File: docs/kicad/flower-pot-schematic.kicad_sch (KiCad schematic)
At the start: 14 parts, among them J1 Raspberry_Pi_2_3, K1 SRD-05VDC-SL-C, M1 Motor_DC, SW1 SW_Push, U1 MCP3202, U2 DHT11, U3 keyestudio_Ks0049

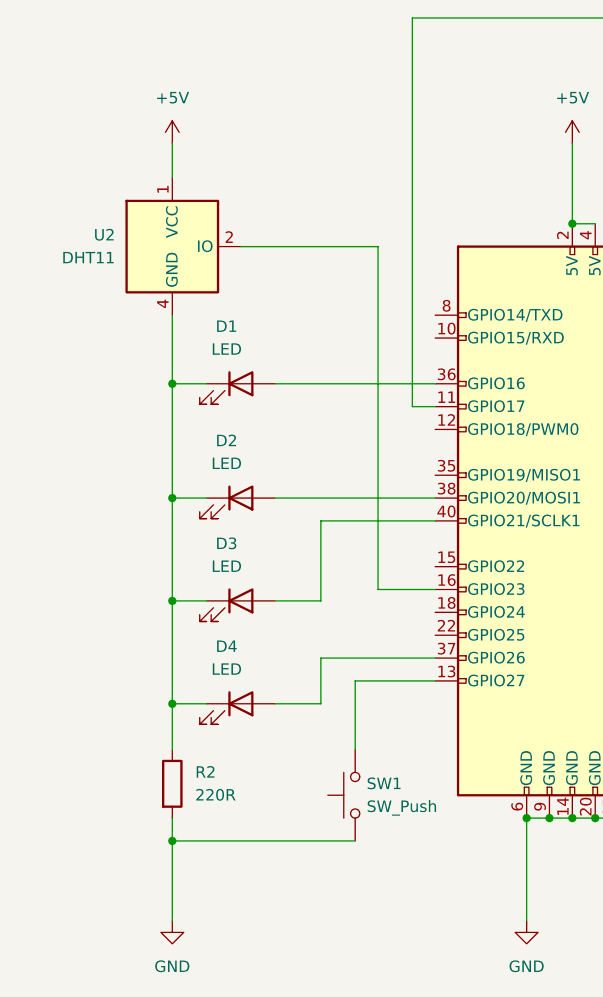
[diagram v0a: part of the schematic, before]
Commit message: fix bad connection on u2
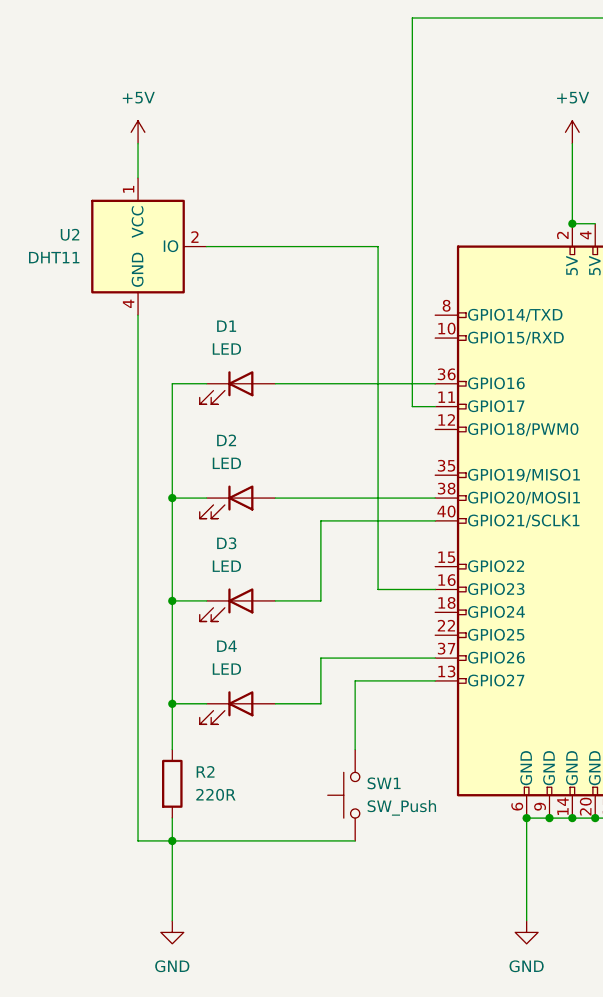
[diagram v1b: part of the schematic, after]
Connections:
- net GND: now also U2.4 (GND)
- net at D1.1 (K), D2.1 (K), D3.1 (K)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: no longer U2.4 (GND)
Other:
- moved on the sheet: U2
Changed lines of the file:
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@@
   (junction (at 81.28 41.91) (diameter 0) (color 0 0 0 0)
   )
-  (junction (at 29.21 59.69) (diameter 0) (color 0 0 0 0)
-  )
   (junction (at 118.11 45.72) (diameter 0) (color 0 0 0 0)
   )
@@
     (stroke (width 0) (type default) (color 0 0 0 0))
   )
-  (wire (pts (xy 29.21 33.02) (xy 29.21 36.83))
+  (wire (pts (xy 25.4 33.02) (xy 25.4 36.83))
     (stroke (width 0) (type default) (color 0 0 0 0))
   )
@@
     (stroke (width 0) (type default) (color 0 0 0 0))
   )
+  (wire (pts (xy 25.4 110.49) (xy 29.21 110.49))
+    (stroke (width 0) (type default) (color 0 0 0 0))
+  )
   (wire (pts (xy 137.16 97.79) (xy 137.16 107.95))
     (stroke (width 0) (type default) (color 0 0 0 0))
@@
     (stroke (width 0) (type default) (color 0 0 0 0))
   )
+  (wire (pts (xy 25.4 52.07) (xy 25.4 110.49))
+    (stroke (width 0) (type default) (color 0 0 0 0))
+  )
   (wire (pts (xy 29.21 107.95) (xy 29.21 110.49))
     (stroke (width 0) (type default) (color 0 0 0 0))
   )
-  (wire (pts (xy 36.83 44.45) (xy 52.07 44.45))
+  (wire (pts (xy 33.02 44.45) (xy 52.07 44.45))
     (stroke (width 0) (type default) (color 0 0 0 0))
   )
@@
   )
   (wire (pts (xy 58.42 92.71) (xy 49.53 92.71))
-    (stroke (width 0) (type default) (color 0 0 0 0))
-  )
-  (wire (pts (xy 29.21 52.07) (xy 29.21 59.69))
     (stroke (width 0) (type default) (color 0 0 0 0))
   )
@@
     (pin "2")
   )
-  (symbol (lib_id "power:+5V") (at 29.21 33.02 0) (unit 1)
-    (in_bom yes) (on_board yes) (fields_autoplaced)
-    (property "Reference" "#PWR?" (id 0) (at 29.21 36.83 0)
-      (effects (font (size 1.27 1.27)) hide)
-    )
-    (property "Value" "+5V" (id 1) (at 29.21 27.94 0))
-    (property "Footprint" "" (id 2) (at 29.21 33.02 0)
-      (effects (font (size 1.27 1.27)) hide)
-    )
-    (property "Datasheet" "" (id 3) (at 29.21 33.02 0)
-      (effects (font (size 1.27 1.27)) hide)
-    )
-    (pin "1")
-  )
-  (symbol (lib_id "Sensor:DHT11") (at 29.21 44.45 0) (unit 1)
-    (in_bom yes) (on_board yes) (fields_autoplaced)
-    (property "Reference" "U2" (id 0) (at 22.86 43.1799 0)
-      (effects (font (size 1.27 1.27)) (justify right))
-    )
-    (property "Value" "DHT11" (id 1) (at 22.86 45.7199 0)
-      (effects (font (size 1.27 1.27)) (justify right))
-    )
-    (property "Footprint" "Sensor:Aosong_DHT11_5.5x12.0_P2.54mm" (id 2) (at 29.21 54.61 0)
-      (effects (font (size 1.27 1.27)) hide)
-    )
-    (property "Datasheet" "http://akizukidenshi.com/download/ds/aosong/DHT11.pdf" (id 3) (at 33.02 38.1 0)
-      (effects (font (size 1.27 1.27)) hide)
-    )
+  (symbol (lib_id "power:+5V") (at 25.4 33.02 0) (unit 1)
+    (in_bom yes) (on_board yes) (fields_autoplaced)
+    (property "Reference" "#PWR?" (id 0) (at 25.4 36.83 0)
+      (effects (font (size 1.27 1.27)) hide)
+    )
+    (property "Value" "+5V" (id 1) (at 25.4 27.94 0))
+    (property "Footprint" "" (id 2) (at 25.4 33.02 0)
+      (effects (font (size 1.27 1.27)) hide)
+    )
+    (property "Datasheet" "" (id 3) (at 25.4 33.02 0)
+      (effects (font (size 1.27 1.27)) hide)
+    )
+    (pin "1")
+  )
+  (symbol (lib_id "Sensor:DHT11") (at 25.4 44.45 0) (unit 1)
+    (in_bom yes) (on_board yes) (fields_autoplaced)
+    (property "Reference" "U2" (id 0) (at 19.05 43.1799 0)
+      (effects (font (size 1.27 1.27)) (justify right))
+    )
+    (property "Value" "DHT11" (id 1) (at 19.05 45.7199 0)
+      (effects (font (size 1.27 1.27)) (justify right))
+    )
+    (property "Footprint" "Sensor:Aosong_DHT11_5.5x12.0_P2.54mm" (id 2) (at 25.4 54.61 0)
+      (effects (font (size 1.27 1.27)) hide)
+    )
+    (property "Datasheet" "http://akizukidenshi.com/download/ds/aosong/DHT11.pdf" (id 3) (at 29.21 38.1 0)
+      (effects (font (size 1.27 1.27)) hide)
+    )

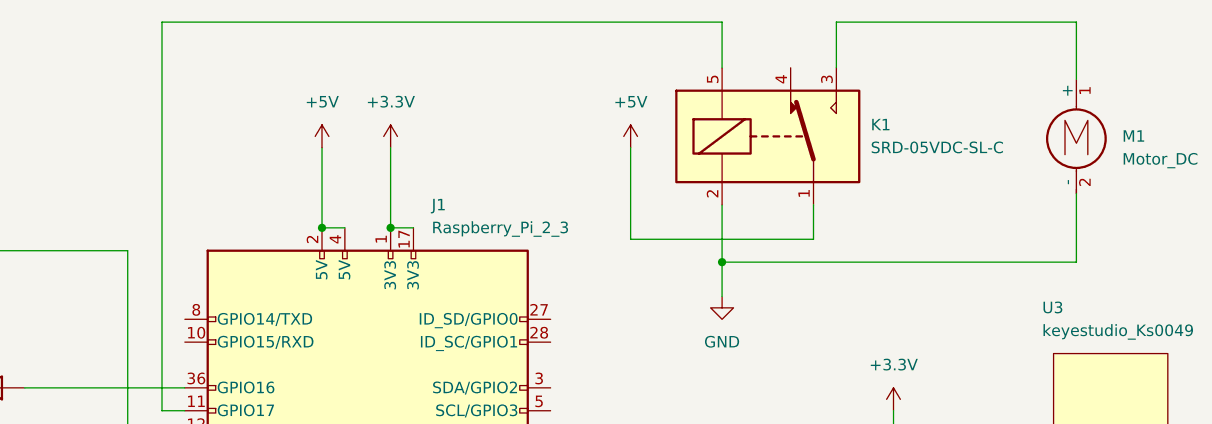
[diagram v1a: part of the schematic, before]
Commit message: add diode to relay, add database, fix element missing error
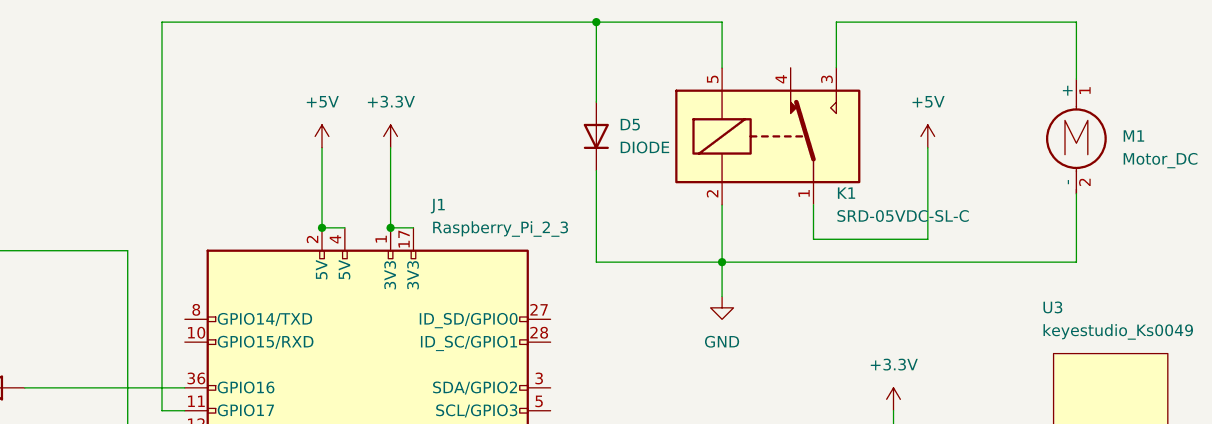
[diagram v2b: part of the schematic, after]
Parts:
- added D5: DIODE, symbol Simulation_SPICE:DIODE
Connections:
- net GND: now also D5.2 (K)
- net at J1.11 (GPIO17), K1.5: now also D5.1 (A)
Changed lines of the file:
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@@
   (junction (at 71.12 107.95) (diameter 0) (color 0 0 0 0)
   )
+  (junction (at 104.14 19.05) (diameter 0) (color 0 0 0 0)
+  )
   (junction (at 175.26 78.74) (diameter 0) (color 0 0 0 0)
   )
@@
     (stroke (width 0) (type default) (color 0 0 0 0))
   )
-  (wire (pts (xy 55.88 19.05) (xy 118.11 19.05))
+  (wire (pts (xy 55.88 19.05) (xy 104.14 19.05))
     (stroke (width 0) (type default) (color 0 0 0 0))
   )
@@
     (stroke (width 0) (type default) (color 0 0 0 0))
   )
+  (wire (pts (xy 104.14 45.72) (xy 118.11 45.72))
+    (stroke (width 0) (type default) (color 0 0 0 0))
+  )
   (wire (pts (xy 118.11 39.37) (xy 118.11 45.72))
     (stroke (width 0) (type default) (color 0 0 0 0))
@@
     (stroke (width 0) (type default) (color 0 0 0 0))
   )
-  (wire (pts (xy 107.95 43.18) (xy 107.95 33.02))
+  (wire (pts (xy 140.97 43.18) (xy 140.97 33.02))
     (stroke (width 0) (type default) (color 0 0 0 0))
   )
@@
     (stroke (width 0) (type default) (color 0 0 0 0))
   )
+  (wire (pts (xy 104.14 19.05) (xy 104.14 27.94))
+    (stroke (width 0) (type default) (color 0 0 0 0))
+  )
   (wire (pts (xy 106.68 80.01) (xy 106.68 90.17))
     (stroke (width 0) (type default) (color 0 0 0 0))
@@
     (stroke (width 0) (type default) (color 0 0 0 0))
   )
+  (wire (pts (xy 104.14 35.56) (xy 104.14 45.72))
+    (stroke (width 0) (type default) (color 0 0 0 0))
+  )
   (wire (pts (xy 29.21 59.69) (xy 33.02 59.69))
     (stroke (width 0) (type default) (color 0 0 0 0))
   )
+  (wire (pts (xy 104.14 19.05) (xy 118.11 19.05))
+    (stroke (width 0) (type default) (color 0 0 0 0))
+  )
   (wire (pts (xy 149.86 90.17) (xy 156.21 90.17))
     (stroke (width 0) (type default) (color 0 0 0 0))
@@
     (stroke (width 0) (type default) (color 0 0 0 0))
   )
-  (wire (pts (xy 128.27 43.18) (xy 107.95 43.18))
+  (wire (pts (xy 128.27 43.18) (xy 140.97 43.18))
     (stroke (width 0) (type default) (color 0 0 0 0))
   )
@@
   )
   (symbol (lib_id "Relay:SANYOU_SRD_Form_C") (at 123.19 31.75 0) (unit 1)
-    (in_bom yes) (on_board yes) (fields_autoplaced)
-    (property "Reference" "K1" (id 0) (at 134.62 30.4799 0)
-      (effects (font (size 1.27 1.27)) (justify left))
-    )
-    (property "Value" "SRD-05VDC-SL-C" (id 1) (at 134.62 33.0199 0)
+    (in_bom yes) (on_board yes)
+    (property "Reference" "K1" (id 0) (at 130.81 38.1 0)
+      (effects (font (size 1.27 1.27)) (justify left))
+    )
+    (property "Value" "SRD-05VDC-SL-C" (id 1) (at 130.81 40.64 0)
       (effects (font (size 1.27 1.27)) (justify left))
     )
@@
     (pin "2")
   )
-  (symbol (lib_id "power:+5V") (at 107.95 33.02 0) (unit 1)
-    (in_bom yes) (on_board yes) (fields_autoplaced)
-    (property "Reference" "#PWR?" (id 0) (at 107.95 36.83 0)
-      (effects (font (size 1.27 1.27)) hide)
-    )
-    (property "Value" "+5V" (id 1) (at 107.95 27.94 0))
-    (property "Footprint" "" (id 2) (at 107.95 33.02 0)
-      (effects (font (size 1.27 1.27)) hide)
-    )
-    (property "Datasheet" "" (id 3) (at 107.95 33.02 0)
+  (symbol (lib_id "power:+5V") (at 140.97 33.02 0) (unit 1)
+    (in_bom yes) (on_board yes) (fields_autoplaced)
+    (property "Reference" "#PWR?" (id 0) (at 140.97 36.83 0)
+      (effects (font (size 1.27 1.27)) hide)
+    )
+    (property "Value" "+5V" (id 1) (at 140.97 27.94 0))
+    (property "Footprint" "" (id 2) (at 140.97 33.02 0)
+      (effects (font (size 1.27 1.27)) hide)
+    )
+    (property "Datasheet" "" (id 3) (at 140.97 33.02 0)
       (effects (font (size 1.27 1.27)) hide)
     )
@@
     (pin "")
   )
+  (symbol (lib_id "Simulation_SPICE:DIODE") (at 104.14 31.75 270) (unit 1)
+    (in_bom yes) (on_board yes) (fields_autoplaced)
+    (property "Reference" "D5" (id 0) (at 106.68 30.4799 90)
+      (effects (font (size 1.27 1.27)) (justify left))
+    )
+    (property "Value" "DIODE" (id 1) (at 106.68 33.0199 90)
+      (effects (font (size 1.27 1.27)) (justify left))
+    )
+    (property "Footprint" "" (id 2) (at 104.14 31.75 0)
+      (effects (font (size 1.27 1.27)) hide)
+    )
+    (property "Datasheet" "~" (id 3) (at 104.14 31.75 0)
+      (effects (font (size 1.27 1.27)) hide)
+    )
+    (property "Spice_Netlist_Enabled" "Y" (id 4) (at 104.14 31.75 0)
+      (effects (font (size 1.27 1.27)) (justify left) hide)
+    )
+    (property "Spice_Primitive" "D" (id 5) (at 104.14 31.75 0)
+      (effects (font (size 1.27 1.27)) (justify left) hide)
+    )
+    (pin "1")
+    (pin "2")
+  )
   (symbol (lib_id "power:GND") (at 118.11 49.53 0) (unit 1)
     (in_bom yes) (on_board yes) (fields_autoplaced)
@@
       (reference "D4") (unit 1) (value "LED") (footprint "")
     )
+    (path "/b8c6f8c4-8e27-4ab6-9e28-8a3ba0a2ee1c"
+      (reference "D5") (unit 1) (value "DIODE") (footprint "")
+    )
     (path "/00e27eb1-22fb-4865-a5bb-081fb730ae76"
